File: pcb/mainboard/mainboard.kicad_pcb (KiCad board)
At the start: 2 copper layers, 87.6 x 63.1 mm, 64 parts, among them J1 V_IN, J2 Conn_01x02, J3 Control Board, J4 M1, J5 M2, J6 Conn_01x02, J7 TIP, K1 SANYOU_SRD_Form_C, Q1 NMOS, Q2 NMOS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

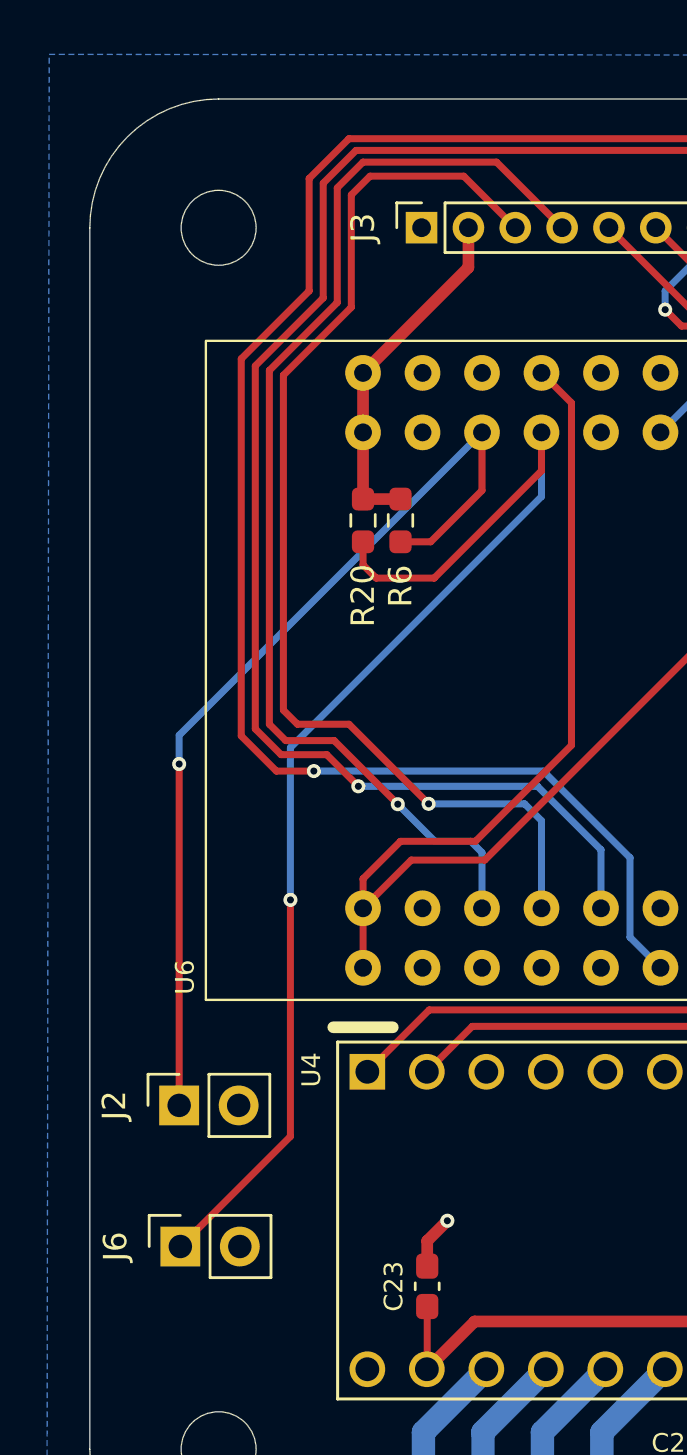
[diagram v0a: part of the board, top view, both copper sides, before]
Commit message: Change Limit Switch Connectors
Change from 2 pin to 3 pin connectors
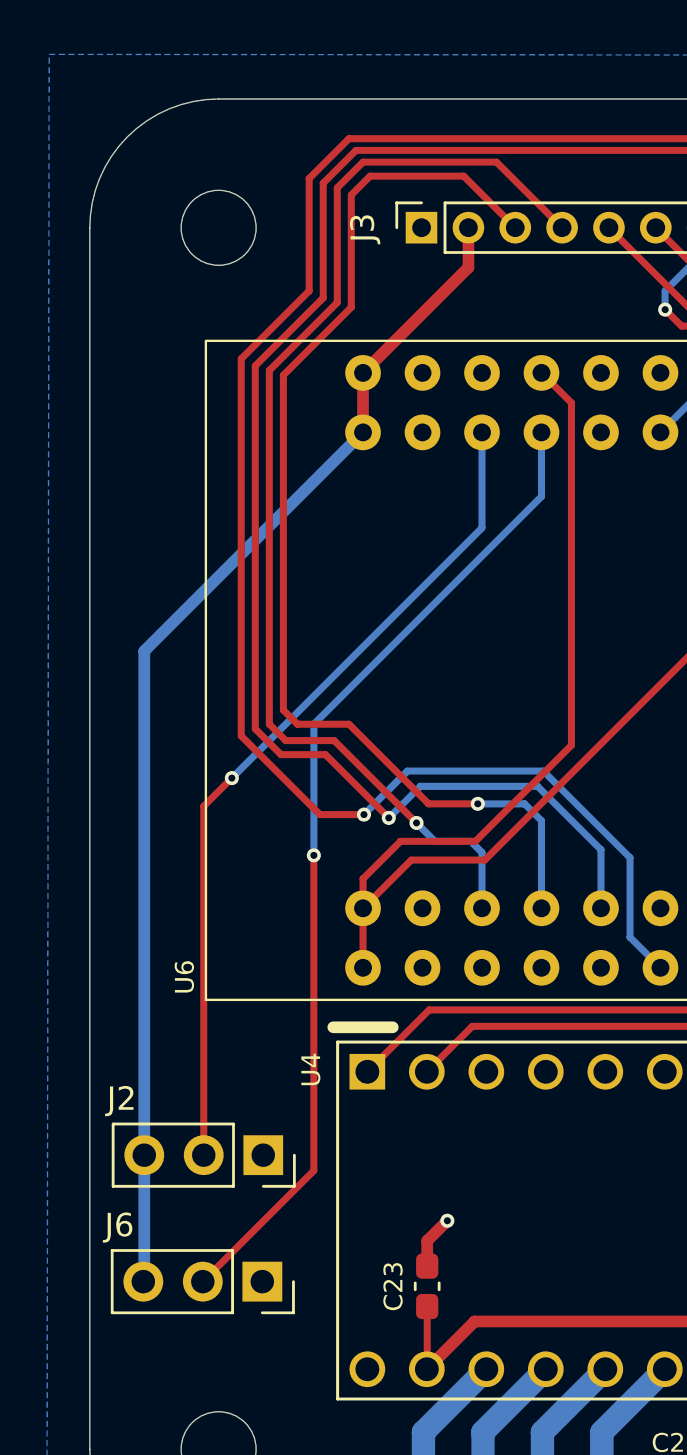
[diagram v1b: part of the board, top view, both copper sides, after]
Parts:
- removed R20, R6: 10k, Resistor_SMD:R_0603_1608Metric_Pad0.98x0.95mm_HandSolder
- J2, J6: value Conn_01x02 -> Conn_01x03; footprint Connector_PinSocket_2.54mm:PinSocket_1x02_P2.54mm_Vertical -> Connector_PinSocket_2.54mm:PinSocket_1x03_P2.54mm_Vertical
- moved J2 4.17 mm to (104.1, 107.7), turned to -90 degrees
- moved J6 3.81 mm to (104.1, 113.1), turned to -90 degrees
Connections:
- J2 pad 1: LIMIT_SWITCH_1 -> GND
- J2 pad 2: GND -> LIMIT_SWITCH_1
- J6 pad 1: LIMIT_SWITCH_2 -> GND
- J6 pad 2: GND -> LIMIT_SWITCH_2
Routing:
- net +3.3V: track 15.1 -> 50.7 mm
- net LIMIT_SWITCH_2: track 53.5 -> 42.3 mm
- net LIMIT_SWITCH_1: track 41.0 -> 35.8 mm
- net ENC_SIG_B: track 74.1 -> 75.6 mm
- net ENC_SIG_A: track 66.0 -> 67.2 mm
